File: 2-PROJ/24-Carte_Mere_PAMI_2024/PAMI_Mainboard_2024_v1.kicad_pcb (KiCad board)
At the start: 2 copper layers, 75 x 75 mm, 37 parts, among them J1 Conn_01x08, J2 Conn_01x03, J3 USB_A, J4 Conn_01x03, J5 Conn_01x02, J6 Conn_01x04, J7 Conn_01x03, SW1 SW_DIP_x04, U3 MCP2515-xST, U4 MCP2551-I-SN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

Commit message: Carte Mère PAMI - Work In Progress
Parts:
- added J10: Conn_01x03, Connector_PinHeader_2.54mm:PinHeader_1x03_P2.54mm_Vertical, F.Cu at (110.2, 108.0)
- added J11: Conn_01x03, Connector_PinHeader_2.54mm:PinHeader_1x03_P2.54mm_Vertical, F.Cu at (110.2, 105.4)
- added J12: Conn_01x03, Connector_PinHeader_2.54mm:PinHeader_1x03_P2.54mm_Vertical, F.Cu at (110.2, 86.4)
- added J13: Conn_01x03, Connector_PinHeader_2.54mm:PinHeader_1x03_P2.54mm_Vertical, F.Cu at (110.2, 83.8)
- added J14: Conn_01x03, Connector_PinHeader_2.54mm:PinHeader_1x03_P2.54mm_Vertical, F.Cu at (110.2, 81.3)
- added J15: Conn_01x03, Connector_PinHeader_2.54mm:PinHeader_1x03_P2.54mm_Vertical, F.Cu at (110.2, 78.7)
- added J16: Conn_01x03, Connector_PinHeader_2.54mm:PinHeader_1x03_P2.54mm_Vertical, F.Cu at (184.8, 113.0)
- added J17: Conn_01x03, Connector_PinHeader_2.54mm:PinHeader_1x03_P2.54mm_Vertical, F.Cu at (184.8, 110.5)
- added J18: Conn_01x03, Connector_PinHeader_2.54mm:PinHeader_1x03_P2.54mm_Vertical, F.Cu at (184.8, 108.0)
- added J19: Conn_01x03, Connector_PinHeader_2.54mm:PinHeader_1x03_P2.54mm_Vertical, F.Cu at (184.8, 105.4)
- added J20: Conn_01x03, Connector_PinHeader_2.54mm:PinHeader_1x03_P2.54mm_Vertical, F.Cu at (184.8, 86.4)
- added J21: Conn_01x03, Connector_PinHeader_2.54mm:PinHeader_1x03_P2.54mm_Vertical, F.Cu at (184.8, 83.8)
- added J22: Conn_01x03, Connector_PinHeader_2.54mm:PinHeader_1x03_P2.54mm_Vertical, F.Cu at (184.8, 81.3)
- added J23: Conn_01x03, Connector_PinHeader_2.54mm:PinHeader_1x03_P2.54mm_Vertical, F.Cu at (184.8, 78.7)
- added J24: Conn_01x06, Connector_PinSocket_2.54mm:PinSocket_1x06_P2.54mm_Vertical, B.Cu at (148.8, 130.2)
- added J25: Conn_02x05_Odd_Even, ConnectorsEvo:690357281076, F.Cu at (171.8, 101.4)
- added J8: Conn_01x03, Connector_PinHeader_2.54mm:PinHeader_1x03_P2.54mm_Vertical, F.Cu at (110.2, 113.0)
- added J9: Conn_01x03, Connector_PinHeader_2.54mm:PinHeader_1x03_P2.54mm_Vertical, F.Cu at (110.2, 110.5)
- added R15: 120, Resistor_SMD:R_0603_1608Metric_Pad0.98x0.95mm_HandSolder, F.Cu at (162.7, 101.6)
- added SW2: SW_DPST_x2, Connector_PinHeader_2.54mm:PinHeader_1x03_P2.54mm_Vertical, B.Cu at (125.1, 74.3)
- J2, J4, J6, SW1: moved to B.Cu
- moved J6 102.7 mm to (182.7, 99.8)
- moved J2 74.3 mm to (159.1, 130.2), turned to 90 degrees
- moved C15 68.7 mm to (157.4, 126.6), turned to -90 degrees
- moved C14 68.2 mm to (155.0, 127.6), turned to 0 degrees
- moved R8 66.3 mm to (155.0, 126.1), turned to 0 degrees
- moved R7 64.4 mm to (155.0, 124.5), turned to 0 degrees
- moved J7 54.1 mm to (143.6, 122.9), turned to 180 degrees
- moved R14 31.2 mm to (152.0, 88.5), turned to 0 degrees
- moved C7 29.4 mm to (152.3, 91.4), turned to 0 degrees
- moved J5 27.9 mm to (165.2, 100.3)
- moved C5 25.6 mm to (147.8, 87.6), turned to 0 degrees
- moved R3 20.8 mm to (148.8, 94.9), turned to 0 degrees
- moved U1 20.6 mm to (147.4, 91.3), turned to 180 degrees
- moved R2 14.2 mm to (145.5, 94.9), turned to 180 degrees
- moved C3 14.1 mm to (140.6, 105.0), turned to 90 degrees
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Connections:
- net /CAN/INT renamed /INT_CAN
- net /SX1509/INT renamed /INT_SX
- J1 pad 8: Net-(J1-Pin_8) -> /+5V_IN
- J7 pad 1: +5V -> GND
- J7 pad 2: GND -> +5V
- R10 pad 1: Net-(R10-Pad1) -> Net-(RP1-GPIO27)
- R11 pad 1: Net-(R11-Pad1) -> Net-(RP1-GPIO23)
- R12 pad 1: Net-(R12-Pad1) -> Net-(RP1-GPIO22)
- R9 pad 1: Net-(R9-Pad1) -> Net-(RP1-GPIO4/GPCLK0)
- RP1 pad 10: unconnected-(RP1-GPIO15/UART_RX-Pad10) -> Net-(J24-Pin_4)
- RP1 pad 13: unconnected-(RP1-GPIO27-Pad13) -> Net-(RP1-GPIO27)
- RP1 pad 15: unconnected-(RP1-GPIO22-Pad15) -> Net-(RP1-GPIO22)
- RP1 pad 16: unconnected-(RP1-GPIO23-Pad16) -> Net-(RP1-GPIO23)
- RP1 pad 18: unconnected-(RP1-GPIO24-Pad18) -> /SIDE
- RP1 pad 26: unconnected-(RP1-GPIO7/SPI0_CE1-Pad26) -> /CaptTOR_1
- RP1 pad 29: unconnected-(RP1-GPIO5/GPCLK1-Pad29) -> /CaptTOR_2
- RP1 pad 7: unconnected-(RP1-GPIO4/GPCLK0-Pad7) -> Net-(RP1-GPIO4/GPCLK0)
- RP1 pad 8: unconnected-(RP1-GPIO14/UART_TX-Pad8) -> Net-(J24-Pin_5)
- SW1 pad 1: Net-(R9-Pad1) -> Net-(RP1-GPIO22)
- SW1 pad 2: Net-(R10-Pad1) -> Net-(RP1-GPIO23)
- SW1 pad 3: Net-(R11-Pad1) -> Net-(RP1-GPIO27)
- SW1 pad 4: Net-(R12-Pad1) -> Net-(RP1-GPIO4/GPCLK0)
- Y1 pad 1: Net-(U3-OSC2) -> Net-(U3-OSC1)
- Y1 pad 2: Net-(U3-OSC1) -> Net-(U3-OSC2)
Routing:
- net +5P: track 0.00 -> 215.8 mm
- net +3.3VP: track 36.6 -> 133.1 mm, vias 0 -> 8
- net /+5V_IN: track 0.00 -> 77.7 mm
- net /SX1509/SDA: track 2.01 -> 71.5 mm, vias 0 -> 2
- net /SX1509/SCL: track 1.84 -> 71.2 mm, vias 0 -> 2
- net /SX1509/SX_IO_0: track 6.59 -> 48.6 mm
- net /SX1509/SX_IO_1: track 5.44 -> 45.7 mm
- net Net-(RP1-GPIO23): track 0.00 -> 39.0 mm
- net Net-(RP1-GPIO4/GPCLK0): track 0.00 -> 38.5 mm
- net /SX1509/SX_IO_2: track 4.60 -> 43.0 mm
- net Net-(RP1-GPIO27): track 0.00 -> 36.5 mm
- net /SX1509/SX_IO_3: track 4.60 -> 41.0 mm
- net Net-(RP1-GPIO22): track 0.00 -> 36.2 mm
- net /SIDE: track 0.00 -> 35.1 mm, vias 0 -> 1
- net /SX1509/SX_IO_15: track 5.07 -> 39.1 mm
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- added copper zone on B.Cu, net +3.3VP
- added copper zone on B.Cu, net +5V
- added copper zone on F.Cu, net GND
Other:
- board size 75 x 75 mm -> 78 x 75 mm

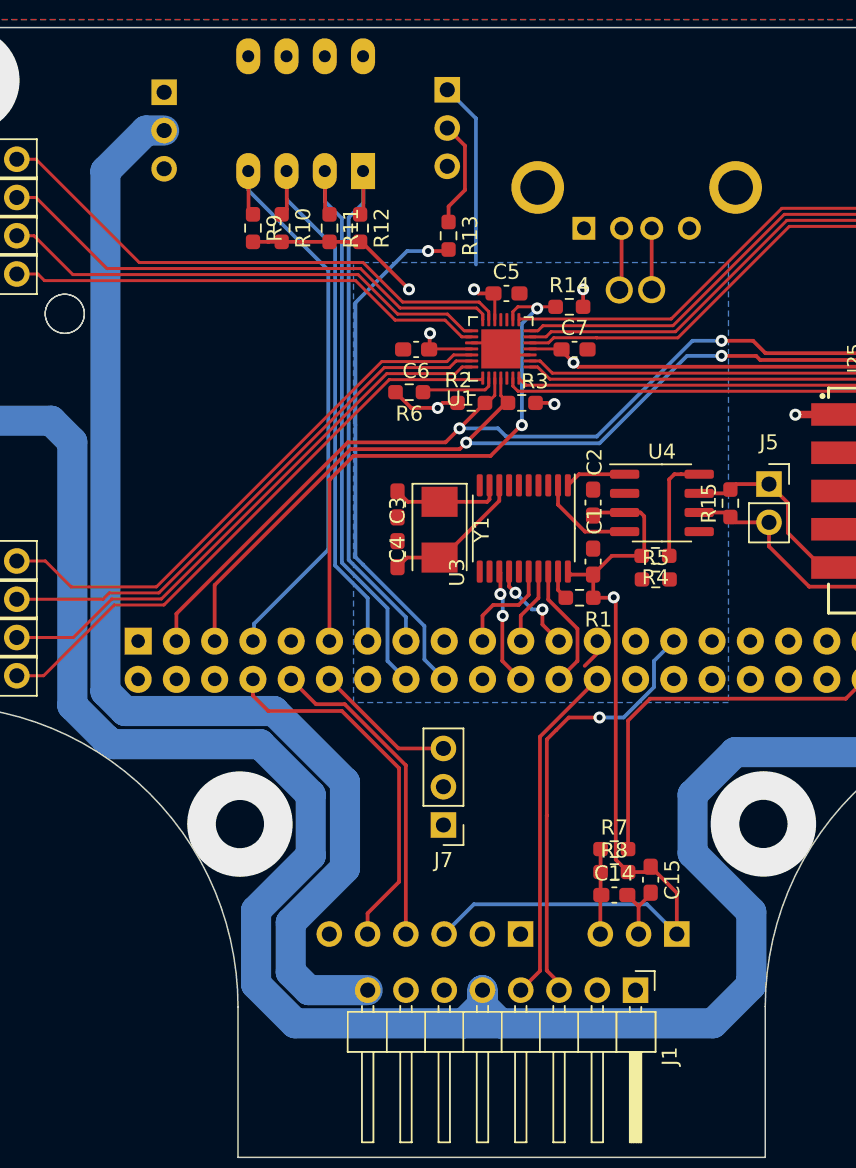
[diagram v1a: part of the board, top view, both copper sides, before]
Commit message: CM PAMI 2024 - Correction interrupteur 5V
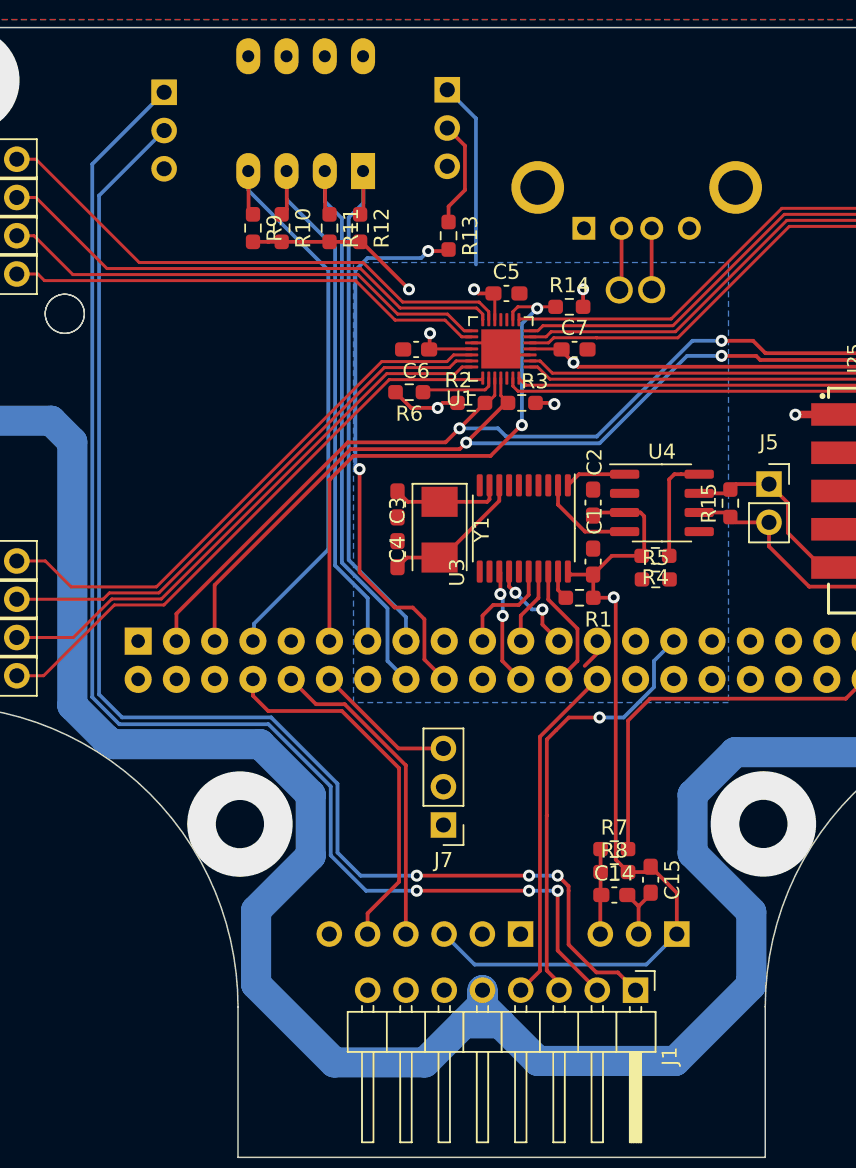
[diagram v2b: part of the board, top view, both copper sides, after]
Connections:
- J1 pad 8: /+5V_IN -> +5V
- SW2 pad 1: +5V -> /EN_5L
- SW2 pad 2: /+5V_IN -> /ALIM_EN_5L
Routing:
- net /EN_5L: track 0.00 -> 88.7 mm, vias 0 -> 3
- net /ALIM_EN_5L: track 0.00 -> 87.9 mm, vias 0 -> 3
- net /+5V_IN: track 77.7 -> 0.00 mm
- net +5P: track 215.8 -> 220.0 mm
- net /SIDE: track 35.1 -> 37.1 mm, vias 1 -> 2

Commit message: CM PAMI 2024 - WIP
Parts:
- added C10: 470uF, Capacitor_THT:C_Radial_D8.0mm_H11.5mm_P3.50mm, F.Cu at (180.0, 102.2)
- added C11: 100nF, Capacitor_SMD:C_0603_1608Metric, F.Cu at (147.6, 124.3)
- added C8: 470uF, Capacitor_THT:C_Radial_D8.0mm_H11.5mm_P3.50mm, B.Cu at (145.0, 120.5)
- added C9: 470uF, Capacitor_THT:C_Radial_D8.0mm_H11.5mm_P3.50mm, F.Cu at (111.2, 102.0)
- added D1: LED, LED_SMD:LED_0603_1608Metric, F.Cu at (120.9, 72.3)
- added H1: MountingHole_Pad, MountingHole:MountingHole_3.2mm_M3_Pad_Via, F.Cu at (130.3, 122.8)
- added H2: MountingHole_Pad, MountingHole:MountingHole_3.2mm_M3_Pad_Via, F.Cu at (164.9, 122.8)
- added H3: MountingHole_Pad, MountingHole:MountingHole_3.2mm_M3_Pad_Via, F.Cu at (183.0, 73.5)
- added H4: MountingHole_Pad, MountingHole:MountingHole_3.2mm_M3_Pad_Via, F.Cu at (112.0, 73.5)
- added R16: 10K, Resistor_SMD:R_0603_1608Metric_Pad0.98x0.95mm_HandSolder, F.Cu at (178.3, 125.8)
- added R17: 10K, Resistor_SMD:R_0603_1608Metric_Pad0.98x0.95mm_HandSolder, F.Cu at (178.2, 129.7)
- added R18: 10K, Resistor_SMD:R_0603_1608Metric_Pad0.98x0.95mm_HandSolder, F.Cu at (176.5, 138.7)
- added R19: 10K, Resistor_SMD:R_0603_1608Metric_Pad0.98x0.95mm_HandSolder, F.Cu at (176.7, 142.7)
- added R20: 68, Resistor_SMD:R_0603_1608Metric_Pad0.98x0.95mm_HandSolder, F.Cu at (152.6, 124.7)
- added R21: R, Resistor_SMD:R_0603_1608Metric, F.Cu at (120.2, 75.7)
- added R22: 10K, Resistor_SMD:R_0603_1608Metric_Pad0.98x0.95mm_HandSolder, F.Cu at (147.0, 67.3)
- added R23: 1K, Resistor_SMD:R_0603_1608Metric_Pad0.98x0.95mm_HandSolder, F.Cu at (103.8, 92.1)
- added R24: 1K, Resistor_SMD:R_0603_1608Metric_Pad0.98x0.95mm_HandSolder, F.Cu at (97.0, 81.8)
- added R25: 1K, Resistor_SMD:R_0603_1608Metric_Pad0.98x0.95mm_HandSolder, F.Cu at (97.5, 86.6)
- added R26: 1K, Resistor_SMD:R_0603_1608Metric_Pad0.98x0.95mm_HandSolder, F.Cu at (99.8, 90.9)
- R13: value 68 -> 1K
- moved J2 50.6 mm to (168.7, 80.5), turned to -90 degrees
- moved C14 48.0 mm to (172.9, 83.1), turned to 180 degrees
- moved R8 45.1 mm to (172.9, 84.6), turned to 180 degrees
- moved C15 44.4 mm to (170.5, 84.1), turned to 90 degrees
- moved R7 42.4 mm to (172.9, 86.1), turned to 180 degrees
- moved J7 15.2 mm to (157.5, 129.2), turned to -90 degrees
- moved J24 1.84 mm to (150.3, 129.2)
- moved J6 1.80 mm to (184.4, 99.2)
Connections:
- J4 pad 1: +3.3VP -> unconnected-(J4-Pin_1-Pad1)
- J7 pad 3: /WS2812B -> Net-(J7-Pin_3)
- R10 pad 1: Net-(RP1-GPIO27) -> Net-(R10-Pad1)
- R11 pad 1: Net-(RP1-GPIO23) -> Net-(R11-Pad1)
- R12 pad 1: Net-(RP1-GPIO22) -> Net-(R12-Pad1)
- R9 pad 1: Net-(RP1-GPIO4/GPCLK0) -> Net-(R26-Pad1)
- RP1 pad 1: +3.3VP -> unconnected-(RP1-3V3-Pad1)
- SW1 pad 1: Net-(RP1-GPIO22) -> Net-(R12-Pad1)
- SW1 pad 2: Net-(RP1-GPIO23) -> Net-(R11-Pad1)
- SW1 pad 3: Net-(RP1-GPIO27) -> Net-(R10-Pad1)
- SW1 pad 4: Net-(RP1-GPIO4/GPCLK0) -> Net-(R26-Pad1)
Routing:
- net +3.3VP: track 133.1 -> 88.4 mm
- net /ALIM_EN_5L: track 87.9 -> 57.2 mm, vias 3 -> 0
- net /EN_5L: track 88.7 -> 60.1 mm, vias 3 -> 0
- net /CaptTOR_2: track 29.1 -> 2.35 mm, vias 1 -> 0
- net /TIRETTE: track 25.4 -> 0.00 mm
- net /CaptTOR_1: track 22.7 -> 5.38 mm
- net unconnected-(J4-Pin_1-Pad1): track 0.00 -> 12.4 mm
- net Net-(J24-Pin_5): track 24.7 -> 12.8 mm
- net Net-(J24-Pin_4): track 21.2 -> 9.97 mm
- net /WS2812B: track 9.47 -> 6.49 mm
- net GND: track 9.41 -> 11.1 mm
- net Net-(U4-Rs): track 7.21 -> 8.79 mm
- net +5P: track 220.0 -> 219.3 mm
- net /CAN/SCK: track 6.39 -> 5.99 mm, vias 2 -> 1
- net /INT_CAN: track 7.77 -> 7.97 mm, vias 2 -> 1
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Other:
- board text added: "Déplacer le connecteur tirette dans cet angle"

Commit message: CM PAMI 2024 - WIP
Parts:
- added D2: WS2812B, LED_SMD:LED_WS2812B_PLCC4_5.0x5.0mm_P3.2mm, B.Cu at (133.8, 142.2)
- added D3: WS2812B, LED_SMD:LED_WS2812B_PLCC4_5.0x5.0mm_P3.2mm, B.Cu at (147.5, 142.2)
- added D4: WS2812B, LED_SMD:LED_WS2812B_PLCC4_5.0x5.0mm_P3.2mm, B.Cu at (161.2, 142.1)
- added R27: 1K, Resistor_SMD:R_0603_1608Metric_Pad0.98x0.95mm_HandSolder, F.Cu at (170.0, 90.2)
- added R28: 1K, Resistor_SMD:R_0603_1608Metric_Pad0.98x0.95mm_HandSolder, F.Cu at (166.7, 89.3)
- added R29: 1K, Resistor_SMD:R_0603_1608Metric_Pad0.98x0.95mm_HandSolder, F.Cu at (170.0, 88.5)
- added R30: 1K, Resistor_SMD:R_0603_1608Metric_Pad0.98x0.95mm_HandSolder, F.Cu at (166.7, 87.7)
- added R31: 1K, Resistor_SMD:R_0603_1608Metric_Pad0.98x0.95mm_HandSolder, F.Cu at (157.1, 93.4)
- added R32: 1K, Resistor_SMD:R_0603_1608Metric_Pad0.98x0.95mm_HandSolder, F.Cu at (160.5, 94.4)
- added R33: 1K, Resistor_SMD:R_0603_1608Metric_Pad0.98x0.95mm_HandSolder, F.Cu at (157.1, 95.3)
- added R34: 1K, Resistor_SMD:R_0603_1608Metric_Pad0.98x0.95mm_HandSolder, F.Cu at (160.5, 96.2)
- added R35: 1K, Resistor_SMD:R_0603_1608Metric_Pad0.98x0.95mm_HandSolder, F.Cu at (91.1, 104.3)
- added R36: 1K, Resistor_SMD:R_0603_1608Metric_Pad0.98x0.95mm_HandSolder, F.Cu at (91.1, 101.8)
- added R37: 1K, Resistor_SMD:R_0603_1608Metric_Pad0.98x0.95mm_HandSolder, F.Cu at (91.1, 99.3)
- added R38: 1K, Resistor_SMD:R_0603_1608Metric_Pad0.98x0.95mm_HandSolder, F.Cu at (91.1, 96.8)
- added R39: 1K, Resistor_SMD:R_0603_1608Metric_Pad0.98x0.95mm_HandSolder, F.Cu at (91.1, 94.3)
- added R40: 1K, Resistor_SMD:R_0603_1608Metric_Pad0.98x0.95mm_HandSolder, F.Cu at (91.1, 91.8)
- added R41: 1K, Resistor_SMD:R_0603_1608Metric_Pad0.98x0.95mm_HandSolder, F.Cu at (91.1, 89.3)
- added R42: 1K, Resistor_SMD:R_0603_1608Metric_Pad0.98x0.95mm_HandSolder, F.Cu at (91.1, 86.8)
- D1: moved to B.Cu
- R21: value R -> 1K
- moved R24 38.8 mm to (135.8, 83.1)
- moved R25 35.9 mm to (133.2, 83.1), turned to -90 degrees
- moved R23 35.8 mm to (138.4, 83.1), turned to -90 degrees
- moved R19 33.3 mm to (157.7, 115.4)
- moved R18 32.2 mm to (154.3, 115.4), turned to 180 degrees
- moved R26 31.9 mm to (130.7, 83.1), turned to -90 degrees
- moved R17 26.0 mm to (163.3, 108.4), turned to 180 degrees
- moved R16 25.3 mm to (159.9, 108.4), turned to 180 degrees
- moved R20 17.6 mm to (137.0, 116.6), turned to 180 degrees
- moved R22 10.4 mm to (140.9, 75.7)
- moved R10 7.62 mm to (133.2, 75.7), turned to 90 degrees
- moved R9 7.62 mm to (130.7, 75.7), turned to 90 degrees
- moved R11 7.62 mm to (135.8, 75.7), turned to 90 degrees
- moved R12 7.61 mm to (138.3, 75.7), turned to 90 degrees
- moved C9 3.41 mm to (114.7, 102.2), turned to 180 degrees
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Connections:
- J10 pad 3: /SX1509/SX_IO_13 -> Net-(J10-Pin_3)
- J11 pad 3: /SX1509/SX_IO_12 -> Net-(J11-Pin_3)
- J12 pad 3: /SX1509/SX_IO_11 -> Net-(J12-Pin_3)
- J13 pad 3: /SX1509/SX_IO_10 -> Net-(J13-Pin_3)
- J14 pad 3: /SX1509/SX_IO_9 -> Net-(J14-Pin_3)
- J15 pad 3: /SX1509/SX_IO_8 -> Net-(J15-Pin_3)
- J16 pad 3: /SX1509/SX_IO_0 -> Net-(J16-Pin_3)
- J17 pad 3: /SX1509/SX_IO_1 -> Net-(J17-Pin_3)
- J18 pad 3: /SX1509/SX_IO_2 -> Net-(J18-Pin_3)
- J19 pad 3: /SX1509/SX_IO_3 -> Net-(J19-Pin_3)
- J20 pad 3: /SX1509/SX_IO_4 -> Net-(J20-Pin_3)
- J21 pad 3: /SX1509/SX_IO_5 -> Net-(J21-Pin_3)
- J22 pad 3: /SX1509/SX_IO_6 -> Net-(J22-Pin_3)
- J23 pad 3: /SX1509/SX_IO_7 -> Net-(J23-Pin_3)
- J7 pad 3: Net-(J7-Pin_3) -> Net-(D4-DOUT)
- J8 pad 3: /SX1509/SX_IO_15 -> Net-(J8-Pin_3)
- J9 pad 3: /SX1509/SX_IO_14 -> Net-(J9-Pin_3)
- R20 pad 1: Net-(J7-Pin_3) -> Net-(D2-DIN)
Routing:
- net +3.3VP: track 88.4 -> 131.1 mm, vias 8 -> 9
- net /ALIM_EN_5L: track 57.2 -> 98.4 mm, vias 0 -> 1
- net /TIRETTE: track 0.00 -> 40.8 mm, vias 0 -> 2
- net /EN_5L: track 60.1 -> 99.6 mm, vias 0 -> 1
- net /SX1509/SX_IO_1: track 45.7 -> 8.41 mm
- net Net-(J17-Pin_3): track 0.00 -> 36.7 mm
- net /SX1509/SX_IO_0: track 48.6 -> 12.9 mm
- net Net-(J16-Pin_3): track 0.00 -> 35.6 mm
- net /SX1509/SX_IO_3: track 41.0 -> 7.36 mm
- net Net-(J19-Pin_3): track 0.00 -> 32.2 mm
- net /SX1509/SX_IO_2: track 43.0 -> 11.0 mm
- net Net-(J18-Pin_3): track 0.00 -> 31.1 mm
- net Net-(D2-DIN): track 0.00 -> 27.9 mm, vias 0 -> 3
- net /CaptTOR_2: track 2.35 -> 28.7 mm
- net /SX1509/SX_IO_7: track 35.5 -> 17.9 mm
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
